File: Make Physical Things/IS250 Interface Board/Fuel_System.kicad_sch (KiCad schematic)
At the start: 1 part, among them U1 AD8400ARZ1

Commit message: Updated Components to have footprints
Added footprints to components that had the wrong ones or were completely missing
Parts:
- U1: footprint SOIC127P600X175-8N -> Package_SO:SOIC-8-1EP_3.9x4.9mm_P1.27mm_EP2.29x3mm
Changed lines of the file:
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@@
     (property "Reference" "U1" (id 0) (at 152.4 82.55 0))
     (property "Value" "AD8400ARZ1" (id 1) (at 152.4 85.09 0))
-    (property "Footprint" "SOIC127P600X175-8N" (id 2) (at 152.4 98.044 0)
+    (property "Footprint" "Package_SO:SOIC-8-1EP_3.9x4.9mm_P1.27mm_EP2.29x3mm" (id 2) (at 152.4 98.044 0)
       (effects (font (size 1.27 1.27)) (justify left bottom) hide)
     )

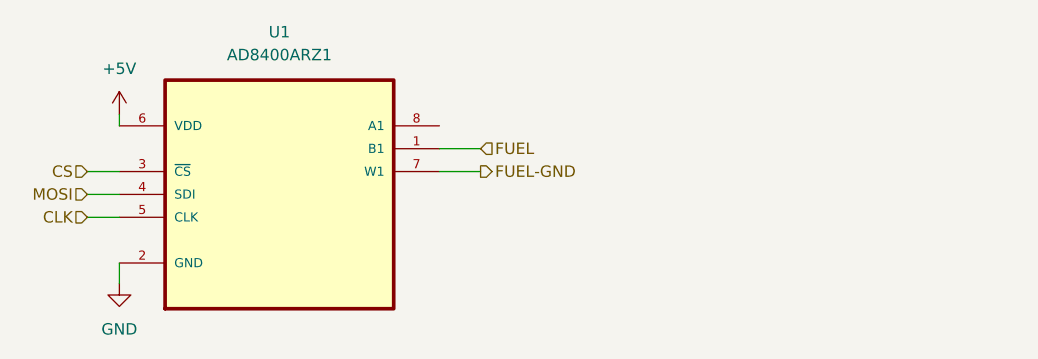
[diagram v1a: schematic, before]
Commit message: Added components to PCB
Got all the components adding onto the PCB, and fixed pinname errors with the 2907
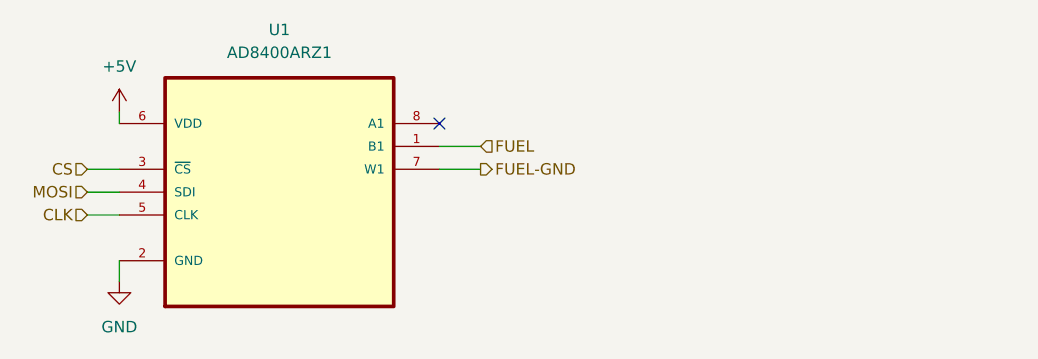
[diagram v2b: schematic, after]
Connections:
- no-connect marks 0 -> 1
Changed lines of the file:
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@@
 (kicad_sch (version 20211123) (generator eeschema)
   (paper "A4")
-  (wire (pts (xy 131.064 103.124) (xy 134.62 103.124))
+  (no_connect (at 170.18 92.71))
+  (wire (pts (xy 131.064 102.87) (xy 134.62 102.87))
     (stroke (width 0) (type default) (color 0 0 0 0))
   )
-  (wire (pts (xy 134.62 108.204) (xy 134.62 110.49))
+  (wire (pts (xy 134.62 107.95) (xy 134.62 110.236))
     (stroke (width 0) (type default) (color 0 0 0 0))
   )
-  (wire (pts (xy 131.064 100.584) (xy 134.62 100.584))
+  (wire (pts (xy 131.064 100.33) (xy 134.62 100.33))
     (stroke (width 0) (type default) (color 0 0 0 0))
   )
-  (wire (pts (xy 131.064 98.044) (xy 134.62 98.044))
+  (wire (pts (xy 131.064 97.79) (xy 134.62 97.79))
     (stroke (width 0) (type default) (color 0 0 0 0))
   )
-  (wire (pts (xy 170.18 95.504) (xy 174.752 95.504))
+  (wire (pts (xy 170.18 95.25) (xy 174.752 95.25))
     (stroke (width 0) (type default) (color 0 0 0 0))
   )
-  (wire (pts (xy 170.18 98.044) (xy 174.752 98.044))
+  (wire (pts (xy 170.18 97.79) (xy 174.752 97.79))
     (stroke (width 0) (type default) (color 0 0 0 0))
   )
-  (wire (pts (xy 134.62 91.694) (xy 134.62 92.964))
+  (wire (pts (xy 134.62 91.44) (xy 134.62 92.71))
     (stroke (width 0) (type default) (color 0 0 0 0))
   )
-  (hierarchical_label "FUEL" (shape input) (at 174.752 95.504 0)
+  (hierarchical_label "FUEL" (shape input) (at 174.752 95.25 0)
     (effects (font (size 1.27 1.27)) (justify left))
   )
-  (hierarchical_label "CS" (shape input) (at 131.064 98.044 180)
+  (hierarchical_label "CS" (shape input) (at 131.064 97.79 180)
     (effects (font (size 1.27 1.27)) (justify right))
   )
-  (hierarchical_label "CLK" (shape input) (at 131.064 103.124 180)
+  (hierarchical_label "CLK" (shape input) (at 131.064 102.87 180)
     (effects (font (size 1.27 1.27)) (justify right))
   )
-  (hierarchical_label "MOSI" (shape input) (at 131.064 100.584 180)
+  (hierarchical_label "MOSI" (shape input) (at 131.064 100.33 180)
     (effects (font (size 1.27 1.27)) (justify right))
   )
-  (hierarchical_label "FUEL-GND" (shape output) (at 174.752 98.044 0)
+  (hierarchical_label "FUEL-GND" (shape output) (at 174.752 97.79 0)
     (effects (font (size 1.27 1.27)) (justify left))
   )
-  (symbol (lib_id "power:+5V") (at 134.62 91.694 0) (unit 1)
+  (symbol (lib_id "power:+5V") (at 134.62 91.44 0) (unit 1)
     (in_bom yes) (on_board yes) (fields_autoplaced)
-    (property "Reference" "#PWR0113" (id 0) (at 134.62 95.504 0)
+    (property "Reference" "#PWR0113" (id 0) (at 134.62 95.25 0)
       (effects (font (size 1.27 1.27)) hide)
     )
-    (property "Value" "+5V" (id 1) (at 134.62 86.614 0))
-    (property "Footprint" "" (id 2) (at 134.62 91.694 0)
+    (property "Value" "+5V" (id 1) (at 134.62 86.36 0))
+    (property "Footprint" "" (id 2) (at 134.62 91.44 0)
       (effects (font (size 1.27 1.27)) hide)
     )
-    (property "Datasheet" "" (id 3) (at 134.62 91.694 0)
+    (property "Datasheet" "" (id 3) (at 134.62 91.44 0)
       (effects (font (size 1.27 1.27)) hide)
     )
     (pin "1")
   )
-  (symbol (lib_id "AD8400ARZ1:AD8400ARZ1") (at 152.4 98.044 0) (unit 1)
+  (symbol (lib_id "AD8400ARZ1:AD8400ARZ1") (at 152.4 97.79 0) (unit 1)
     (in_bom yes) (on_board yes) (fields_autoplaced)
-    (property "Reference" "U1" (id 0) (at 152.4 82.55 0))
-    (property "Value" "AD8400ARZ1" (id 1) (at 152.4 85.09 0))
-    (property "Footprint" "Package_SO:SOIC-8-1EP_3.9x4.9mm_P1.27mm_EP2.29x3mm" (id 2) (at 152.4 98.044 0)
+    (property "Reference" "U1" (id 0) (at 152.4 82.296 0))
+    (property "Value" "AD8400ARZ1" (id 1) (at 152.4 84.836 0))
+    (property "Footprint" "Package_SO:SOIC-8-1EP_3.9x4.9mm_P1.27mm_EP2.29x3mm" (id 2) (at 152.4 97.79 0)
       (effects (font (size 1.27 1.27)) (justify left bottom) hide)
     )
-    (property "Datasheet" "" (id 3) (at 152.4 98.044 0)
+    (property "Datasheet" "" (id 3) (at 152.4 97.79 0)
       (effects (font (size 1.27 1.27)) (justify left bottom) hide)
     )
-    (property "OC_FARNELL" "1661082" (id 4) (at 152.4 98.044 0)
+    (property "OC_FARNELL" "1661082" (id 4) (at 152.4 97.79 0)
       (effects (font (size 1.27 1.27)) (justify left bottom) hide)
     )
-    (property "MPN" "AD8400ARZ1" (id 5) (at 152.4 98.044 0)
+    (property "MPN" "AD8400ARZ1" (id 5) (at 152.4 97.79 0)
       (effects (font (size 1.27 1.27)) (justify left bottom) hide)
     )
-    (property "PACKAGE" "SOIC-8" (id 6) (at 152.4 98.044 0)
+    (property "PACKAGE" "SOIC-8" (id 6) (at 152.4 97.79 0)
       (effects (font (size 1.27 1.27)) (justify left bottom) hide)
     )
-    (property "OC_NEWARK" "19M8905" (id 7) (at 152.4 98.044 0)
+    (property "OC_NEWARK" "19M8905" (id 7) (at 152.4 97.79 0)
       (effects (font (size 1.27 1.27)) (justify left bottom) hide)
     )
-    (property "SUPPLIER" "ANALOG DEVICES" (id 8) (at 152.4 98.044 0)
+    (property "SUPPLIER" "ANALOG DEVICES" (id 8) (at 152.4 97.79 0)
       (effects (font (size 1.27 1.27)) (justify left bottom) hide)
     )
@@
     (pin "8")
   )
-  (symbol (lib_id "power:GND") (at 134.62 110.49 0) (unit 1)
+  (symbol (lib_id "power:GND") (at 134.62 110.236 0) (unit 1)
     (in_bom yes) (on_board yes) (fields_autoplaced)
-    (property "Reference" "#PWR0114" (id 0) (at 134.62 116.84 0)
+    (property "Reference" "#PWR0114" (id 0) (at 134.62 116.586 0)
       (effects (font (size 1.27 1.27)) hide)
     )
-    (property "Value" "GND" (id 1) (at 134.62 115.57 0))
-    (property "Footprint" "" (id 2) (at 134.62 110.49 0)
+    (property "Value" "GND" (id 1) (at 134.62 115.316 0))
+    (property "Footprint" "" (id 2) (at 134.62 110.236 0)
       (effects (font (size 1.27 1.27)) hide)
     )
-    (property "Datasheet" "" (id 3) (at 134.62 110.49 0)
+    (property "Datasheet" "" (id 3) (at 134.62 110.236 0)
       (effects (font (size 1.27 1.27)) hide)
     )

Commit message: Added XT60 and backup fuel resistor
Added an XT60 power connector, and an optional resistor if there isn't an AD8400 connected, so that the fuel gauge will show not empty
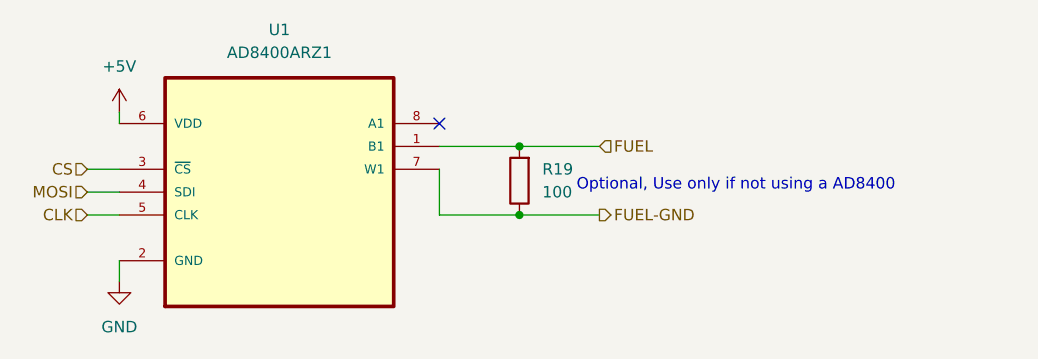
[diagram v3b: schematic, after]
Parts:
- added R19: 100, Resistor_THT:R_Axial_DIN0207_L6.3mm_D2.5mm_P10.16mm_Horizontal, symbol Device:R
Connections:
- net FUEL: now also R19.2
- net FUEL-GND: now also R19.1
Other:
- note added: "Optional, Use only if not using a AD8400"
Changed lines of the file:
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@@
 (kicad_sch (version 20211123) (generator eeschema)
   (paper "A4")
+  (junction (at 179.07 102.87) (diameter 0) (color 0 0 0 0)
+  )
+  (junction (at 179.07 95.25) (diameter 0) (color 0 0 0 0)
+  )
   (no_connect (at 170.18 92.71))
   (wire (pts (xy 131.064 102.87) (xy 134.62 102.87))
@@
     (stroke (width 0) (type default) (color 0 0 0 0))
   )
+  (wire (pts (xy 179.07 95.25) (xy 187.96 95.25))
+    (stroke (width 0) (type default) (color 0 0 0 0))
+  )
+  (wire (pts (xy 170.18 97.79) (xy 170.18 102.87))
+    (stroke (width 0) (type default) (color 0 0 0 0))
+  )
+  (wire (pts (xy 179.07 102.87) (xy 187.96 102.87))
+    (stroke (width 0) (type default) (color 0 0 0 0))
+  )
+  (wire (pts (xy 170.18 102.87) (xy 179.07 102.87))
+    (stroke (width 0) (type default) (color 0 0 0 0))
+  )
   (wire (pts (xy 131.064 97.79) (xy 134.62 97.79))
     (stroke (width 0) (type default) (color 0 0 0 0))
   )
-  (wire (pts (xy 170.18 95.25) (xy 174.752 95.25))
-    (stroke (width 0) (type default) (color 0 0 0 0))
-  )
-  (wire (pts (xy 170.18 97.79) (xy 174.752 97.79))
+  (wire (pts (xy 170.18 95.25) (xy 179.07 95.25))
     (stroke (width 0) (type default) (color 0 0 0 0))
   )
@@
     (stroke (width 0) (type default) (color 0 0 0 0))
   )
-  (hierarchical_label "FUEL" (shape input) (at 174.752 95.25 0)
+  (text "Optional, Use only if not using a AD8400\n" (at 185.42 100.33 0)
+    (effects (font (size 1.27 1.27)) (justify left bottom))
+  )
+  (hierarchical_label "FUEL" (shape input) (at 187.96 95.25 0)
     (effects (font (size 1.27 1.27)) (justify left))
   )
@@
     (effects (font (size 1.27 1.27)) (justify right))
   )
-  (hierarchical_label "FUEL-GND" (shape output) (at 174.752 97.79 0)
+  (hierarchical_label "FUEL-GND" (shape output) (at 187.96 102.87 0)
     (effects (font (size 1.27 1.27)) (justify left))
   )
@@
     (pin "1")
   )
+  (symbol (lib_id "Device:R") (at 179.07 99.06 180) (unit 1)
+    (in_bom yes) (on_board yes) (fields_autoplaced)
+    (property "Reference" "R19" (id 0) (at 181.61 97.7899 0)
+      (effects (font (size 1.27 1.27)) (justify right))
+    )
+    (property "Value" "100" (id 1) (at 181.61 100.3299 0)
+      (effects (font (size 1.27 1.27)) (justify right))
+    )
+    (property "Footprint" "Resistor_THT:R_Axial_DIN0207_L6.3mm_D2.5mm_P10.16mm_Horizontal" (id 2) (at 180.848 99.06 90)
+      (effects (font (size 1.27 1.27)) hide)
+    )
+    (property "Datasheet" "~" (id 3) (at 179.07 99.06 0)
+      (effects (font (size 1.27 1.27)) hide)
+    )
+    (pin "1")
+    (pin "2")
+  )
 )
